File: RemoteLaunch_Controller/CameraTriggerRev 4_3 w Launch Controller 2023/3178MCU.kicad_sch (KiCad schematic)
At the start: 9 parts, among them IC1 3178, J9 Misc

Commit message: Adding Rev4_3 rev
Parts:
- removed J9: Misc, Connector_PinHeader_2.54mm:PinHeader_1x08_P2.54mm_Vertical, symbol CameraTriggerSensorNodeOnly-rescue:Conn_01x08_Female-Connector
- added J9: Conn_01x09_Socket, Connector_PinHeader_2.54mm:PinHeader_1x09_P2.54mm_Vertical, symbol Connector:Conn_01x09_Socket
- D1: value LED Trig -> D_1
- D6: value LED -> D_2
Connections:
- net +3V3: now also J9.9 (Pin_9)
- net A4: now also J9.8 (Pin_8)
- net A5: now also J9.7 (Pin_7)
- net GND: now also J9.1 (Pin_1)
- net MISO: now also J9.4 (Pin_4)
- net MOSI: now also J9.5 (Pin_5)
- net SCK: now also J9.6 (Pin_6)
- net at IC1.14 (D1): now also J9.2 (Pin_2)
- net at IC1.15 (D0): now also J9.3 (Pin_3)
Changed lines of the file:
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@@
   (no_connect (at 80.01 105.41))
   (no_connect (at 95.25 143.51))
-  (wire (pts (xy 55.88 107.95) (xy 85.09 107.95))
+  (wire (pts (xy 60.96 107.95) (xy 85.09 107.95))
     (stroke (width 0) (type default))
   )
@@
     (stroke (width 0) (type default))
   )
-  (wire (pts (xy 55.88 109.22) (xy 55.88 107.95))
+  (wire (pts (xy 60.96 109.22) (xy 60.96 107.95))
     (stroke (width 0) (type default))
   )
@@
     )
   )
-  (symbol (lib_id "power:GND") (at 55.88 109.22 0) (unit 1)
-    (in_bom yes) (on_board yes) (dnp no)
-    (property "Reference" "#PWR01" (at 55.88 115.57 0)
-      (effects (font (size 1.27 1.27)) hide)
-    )
-    (property "Value" "GND" (at 56.007 113.6142 0)
-      (effects (font (size 1.27 1.27)))
-    )
-    (property "Footprint" "" (at 55.88 109.22 0)
-      (effects (font (size 1.27 1.27)) hide)
-    )
-    (property "Datasheet" "" (at 55.88 109.22 0)
+  (symbol (lib_id "power:GND") (at 60.96 109.22 0) (unit 1)
+    (in_bom yes) (on_board yes) (dnp no)
+    (property "Reference" "#PWR01" (at 60.96 115.57 0)
+      (effects (font (size 1.27 1.27)) hide)
+    )
+    (property "Value" "GND" (at 61.087 113.6142 0)
+      (effects (font (size 1.27 1.27)))
+    )
+    (property "Footprint" "" (at 60.96 109.22 0)
+      (effects (font (size 1.27 1.27)) hide)
+    )
+    (property "Datasheet" "" (at 60.96 109.22 0)
       (effects (font (size 1.27 1.27)) hide)
     )
@@
   (symbol (lib_id "CameraTriggerSensorNodeOnly-rescue:+3.3V-power") (at 76.2 100.33 0) (unit 1)
     (in_bom yes) (on_board yes) (dnp no)
-    (property "Reference" "#PWR02" (at 76.2 104.14 0)
+    (property "Reference" "#PWR0101" (at 76.2 104.14 0)
       (effects (font (size 1.27 1.27)) hide)
     )
@@
       (project "CameraTriggerSensorNodeOnly"
         (path "/be0400c2-1232-4f08-847a-2fb9cb6273cc/00000000-0000-0000-0000-0000621ecc98"
-          (reference "#PWR02") (unit 1)
+          (reference "#PWR0101") (unit 1)
         )
       )
@@
       (effects (font (size 1.27 1.27)))
     )
-    (property "Value" "LED Trig" (at 186.8678 72.0344 0)
+    (property "Value" "D_1" (at 186.8678 72.0344 0)
       (effects (font (size 1.27 1.27)))
     )
@@
       (effects (font (size 1.27 1.27)))
     )
-    (property "Value" "LED" (at 181.7878 88.5444 0)
+    (property "Value" "D_2" (at 181.7878 88.5444 0)
       (effects (font (size 1.27 1.27)))
     )
@@
     )
   )
-  (symbol (lib_id "CameraTriggerSensorNodeOnly-rescue:Conn_01x08_Female-Connector") (at 50.8 130.81 180) (unit 1)
-    (in_bom yes) (on_board yes) (dnp no)
-    (property "Reference" "J9" (at 53.5432 114.935 0)
-      (effects (font (size 1.27 1.27)))
-    )
-    (property "Value" "Misc" (at 53.5432 117.2464 0)
-      (effects (font (size 1.27 1.27)))
-    )
-    (property "Footprint" "Connector_PinHeader_2.54mm:PinHeader_1x08_P2.54mm_Vertical" (at 50.8 130.81 0)
-      (effects (font (size 1.27 1.27)) hide)
-    )
-    (property "Datasheet" "~" (at 50.8 130.81 0)
+  (symbol (lib_id "power:GND") (at 55.88 143.51 0) (unit 1)
+    (in_bom yes) (on_board yes) (dnp no)
+    (property "Reference" "#PWR039" (at 55.88 149.86 0)
+      (effects (font (size 1.27 1.27)) hide)
+    )
+    (property "Value" "GND" (at 56.007 147.9042 0)
+      (effects (font (size 1.27 1.27)))
+    )
+    (property "Footprint" "" (at 55.88 143.51 0)
+      (effects (font (size 1.27 1.27)) hide)
+    )
+    (property "Datasheet" "" (at 55.88 143.51 0)
+      (effects (font (size 1.27 1.27)) hide)
+    )
+    (pin "1")
+    (instances
+      (project "CameraTriggerSensorNodeOnly"
+        (path "/be0400c2-1232-4f08-847a-2fb9cb6273cc/00000000-0000-0000-0000-0000621ecc98"
+          (reference "#PWR039") (unit 1)
+        )
+      )
+    )
+  )
+  (symbol (lib_id "Connector:Conn_01x09_Socket") (at 50.8 128.27 180) (unit 1)
+    (in_bom yes) (on_board yes) (dnp no)
+    (property "Reference" "J9" (at 48.26 124.46 0)
+      (effects (font (size 1.27 1.27)))
+    )
+    (property "Value" "Conn_01x09_Socket" (at 51.435 115.57 0)
+      (effects (font (size 1.27 1.27)) hide)
+    )
+    (property "Footprint" "Connector_PinHeader_2.54mm:PinHeader_1x09_P2.54mm_Vertical" (at 50.8 128.27 0)
+      (effects (font (size 1.27 1.27)) hide)
+    )
+    (property "Datasheet" "~" (at 50.8 128.27 0)
       (effects (font (size 1.27 1.27)) hide)
     )
@@
     (pin "7")
     (pin "8")
+    (pin "9")
     (instances
       (project "CameraTriggerSensorNodeOnly"
@@
     )
   )
-  (symbol (lib_id "power:GND") (at 55.88 143.51 0) (unit 1)
-    (in_bom yes) (on_board yes) (dnp no)
-    (property "Reference" "#PWR039" (at 55.88 149.86 0)
-      (effects (font (size 1.27 1.27)) hide)
-    )
-    (property "Value" "GND" (at 56.007 147.9042 0)
-      (effects (font (size 1.27 1.27)))
-    )
-    (property "Footprint" "" (at 55.88 143.51 0)
-      (effects (font (size 1.27 1.27)) hide)
-    )
-    (property "Datasheet" "" (at 55.88 143.51 0)
-      (effects (font (size 1.27 1.27)) hide)
-    )
-    (pin "1")
-    (instances
-      (project "CameraTriggerSensorNodeOnly"
-        (path "/be0400c2-1232-4f08-847a-2fb9cb6273cc/00000000-0000-0000-0000-0000621ecc98"
-          (reference "#PWR039") (unit 1)
-        )
-      )
+  (symbol (lib_id "CameraTriggerSensorNodeOnly-rescue:+3.3V-power") (at 55.88 118.11 0) (unit 1)
+    (in_bom yes) (on_board yes) (dnp no)
+    (property "Reference" "#PWR02" (at 55.88 121.92 0)
+      (effects (font (size 1.27 1.27)) hide)
+    )
+    (property "Value" "+3.3V" (at 56.261 113.7158 0)
+      (effects (font (size 1.27 1.27)))
+    )
+    (property "Footprint" "" (at 55.88 118.11 0)
+      (effects (font (size 1.27 1.27)) hide)
+    )
+    (property "Datasheet" "" (at 55.88 118.11 0)
+      (effects (font (size 1.27 1.27)) hide)
+    )
+    (pin "1")
+    (instances
+      (project "CameraTriggerSensorNodeOnly"
+        (path "/be0400c2-1232-4f08-847a-2fb9cb6273cc/00000000-0000-0000-0000-0000621ecc98"
+          (reference "#PWR02") (unit 1)
+        )
+      )

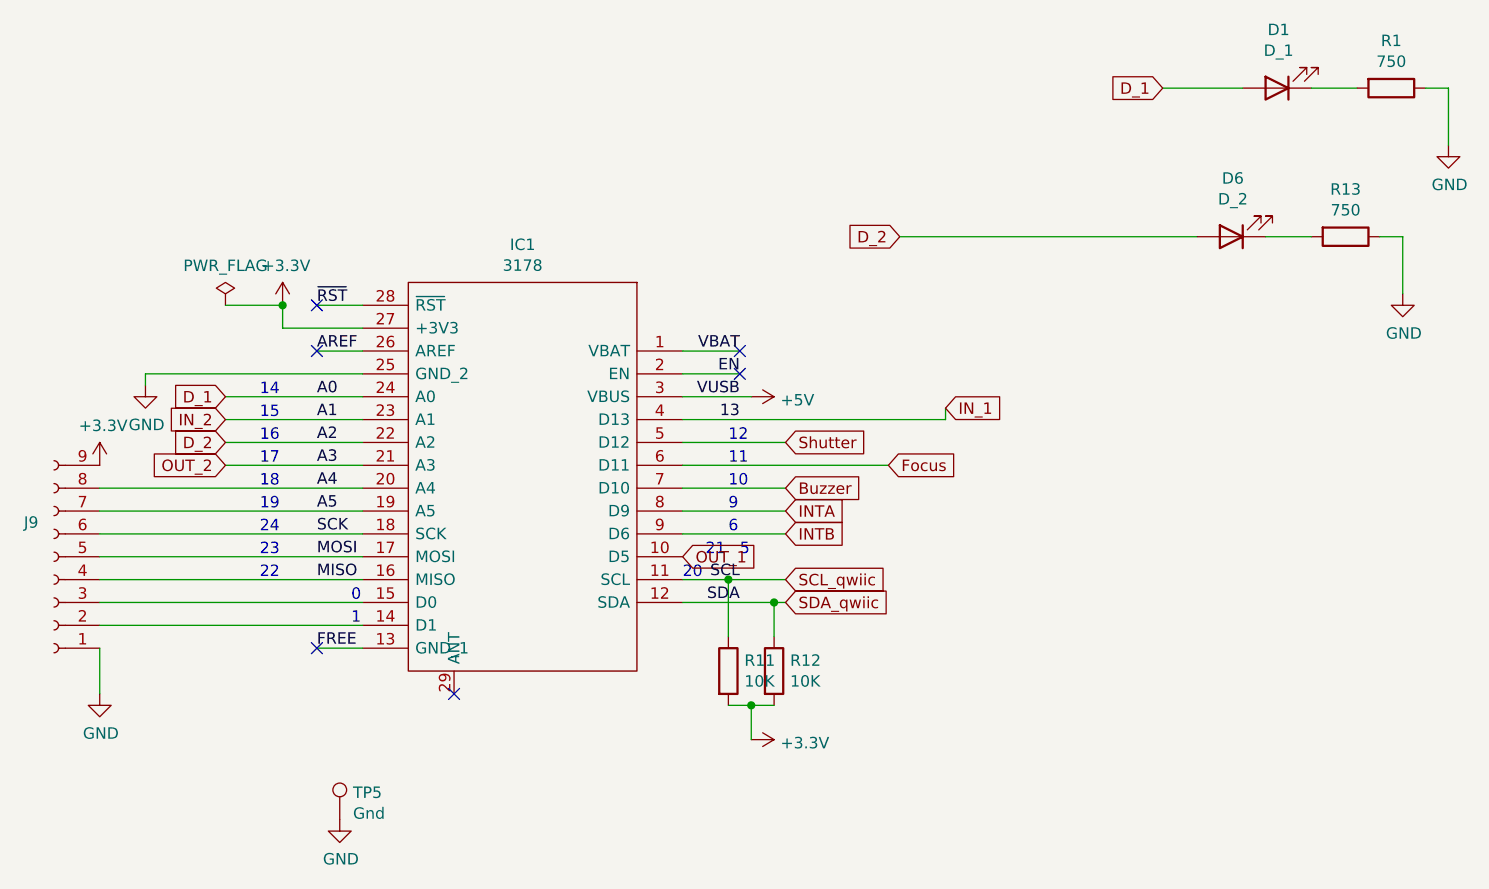
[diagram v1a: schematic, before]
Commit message: Working on adding polling / heartbeat;  Seem to have broken launch
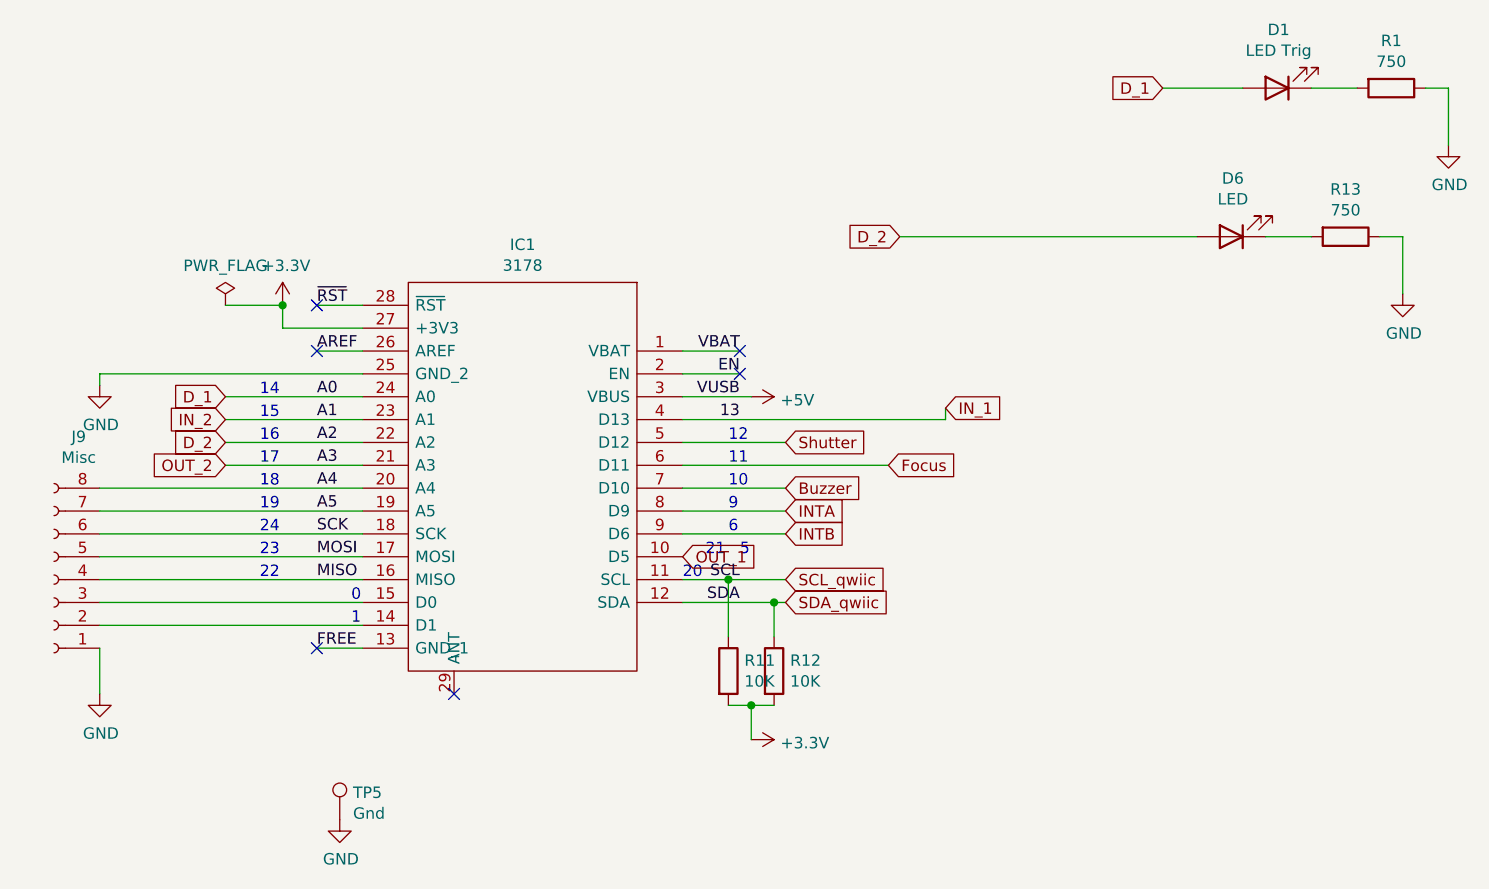
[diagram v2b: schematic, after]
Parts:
- removed J9: Conn_01x09_Socket, Connector_PinHeader_2.54mm:PinHeader_1x09_P2.54mm_Vertical, symbol Connector:Conn_01x09_Socket
- added J9: Misc, Connector_PinHeader_2.54mm:PinHeader_1x08_P2.54mm_Vertical, symbol CameraTriggerSensorNodeOnly-rescue:Conn_01x08_Female-Connector
- D1: value D_1 -> LED Trig
- D6: value D_2 -> LED
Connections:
- net A4: now also J9.8 (Pin_8)
- net A5: now also J9.7 (Pin_7)
- net GND: now also J9.1 (Pin_1)
- net MISO: now also J9.4 (Pin_4)
- net MOSI: now also J9.5 (Pin_5)
- net SCK: now also J9.6 (Pin_6)
- net at IC1.14 (D1): now also J9.2 (Pin_2)
- net at IC1.15 (D0): now also J9.3 (Pin_3)
